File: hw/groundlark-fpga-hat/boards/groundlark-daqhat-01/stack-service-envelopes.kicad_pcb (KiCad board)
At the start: 6 copper layers, 140 x 56 mm, 190 parts, among them J1 Raspberry Pi 40-pin, J130 PI BATTERY 8-18V, J131 SWD / 3V3 REF, J4 FPGA test UART/reset, J80 LSHM-150-04.0-L-DV-A-S-K-TR, J81 LSHM-150-04.0-L-DV-A-S-K-TR, J82 LSHM-130-04.0-L-DV-A-S-K-TR, J83 12V DC / CENTER +, J90 GEO + / - / SHIELD, Q1 2N7002, Q130 2N7002, Q131 2N7002, SW80 FPGA OFF / ON, U1 24LC32A, U100 TMUX1574PWR, U101 TMUX1574PWR, U102 TCA9534PWR, U103 SN74LVC1G10DCKR, U104 TLV809EA30DBZR, U105 TLV809EA30DBZR, U106 SN74LVC1G08DCKR, U11 LSM6DSOTR, U12 LSM6DSOTR, U13 LSM6DSOTR, U130 MSPM0L1105, U131 TPS70933, U132 TPSM53603, U133 TPS22953, U22 ADS122C04, U23 DLVR-F50D, U40 TLV1117LV33DCYR, U41 SN74LVC8T245PWR, U42 SN74LVC8T245PWR, U43 ISO1640BDR, U51 TXU0202DCUR, U52 TLV803EA30DBZR, U80 TPSM53603

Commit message: Add Groundlark GNSS timing, SMA access and calibration workflow
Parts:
- added C146: 4.7u, Groundlark:Capacitor_SMD__C_0805_2012Metric, B.Cu at (71.5, 67.4)
- added C147: 100n, Groundlark:Capacitor_SMD__C_0603_1608Metric, B.Cu at (75.0, 67.4)
- added C148: 47p C0G, Groundlark:GNSS_C0402, B.Cu at (56.4, 65.8)
- added C149: 4.7u, Groundlark:Capacitor_SMD__C_0805_2012Metric, F.Cu at (70.0, 84.0)
- added C150: 4.7u, Groundlark:Capacitor_SMD__C_0805_2012Metric, F.Cu at (78.0, 84.0)
- added D140: PESD5V0F1BL, Groundlark:GNSS_SOD882, F.Cu at (54.0, 71.2)
- added J140: GNSS ANT / 3V3, Groundlark:GNSS_HL_SMA_KWE_02, F.Cu at (54.0, 65.8)
- added L140: 27n, Groundlark:GNSS_L0402, F.Cu at (54.0, 61.5)
- added TP90: GND, Groundlark:TestPoint__TestPoint_Pad_D1.5mm, B.Cu at (56.6, 97.0)
- added TP91: GEO_VCM, Groundlark:TestPoint__TestPoint_Pad_D1.5mm, B.Cu at (54.0, 97.0)
- added TP92: GEO_AVDD, Groundlark:TestPoint__TestPoint_Pad_D1.5mm, B.Cu at (57.3, 90.7)
- added TP93: GEO_DRDY_N, Groundlark:TestPoint__TestPoint_Pad_D1.5mm, B.Cu at (59.2, 88.5)
- added U140: TPS70933, Groundlark:SUP_SOT-23-5, F.Cu at (74.0, 84.0)
- added U21: MAX-M10S-00B, Groundlark:RF_GPS__ublox_MAX, B.Cu at (63.5, 62.5)
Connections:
- J1 pad 18: 18 -> GNSS_PPS
- J80 pad 18: j80-18 -> 18
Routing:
- net GNSS_BIAS: track 0.00 -> 46.1 mm, vias 0 -> 2
- net GND: track 631.4 -> 665.6 mm, vias 141 -> 145
- net PI_5V: track 490.2 -> 519.7 mm, vias 12 -> 15
- net PI_I2C_SCL: track 44.0 -> 73.4 mm, vias 4 -> 2
- net GNSS_PPS: track 0.00 -> 21.5 mm, vias 0 -> 4
- net PI_GEO_DRDY_N: track 62.8 -> 76.0 mm, vias 9 -> 7
- net PI_3V3: track 287.2 -> 298.7 mm
- net GNSS_ANT: track 0.00 -> 10.5 mm
- net PI_I2C_SDA: track 43.6 -> 52.3 mm
- net SPI_MOSI: track 94.2 -> 87.6 mm, vias 13 -> 14
- net IMU3_CS: track 62.6 -> 68.2 mm
- net FPGA_UART_TX: track 83.8 -> 88.4 mm
- net FPGA_RESET_GPIO: track 52.0 -> 56.3 mm, vias 6 -> 8
- net SENS_3V3: track 246.5 -> 242.3 mm
- net SPI_MISO: track 95.9 -> 93.6 mm, vias 20 -> 18
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
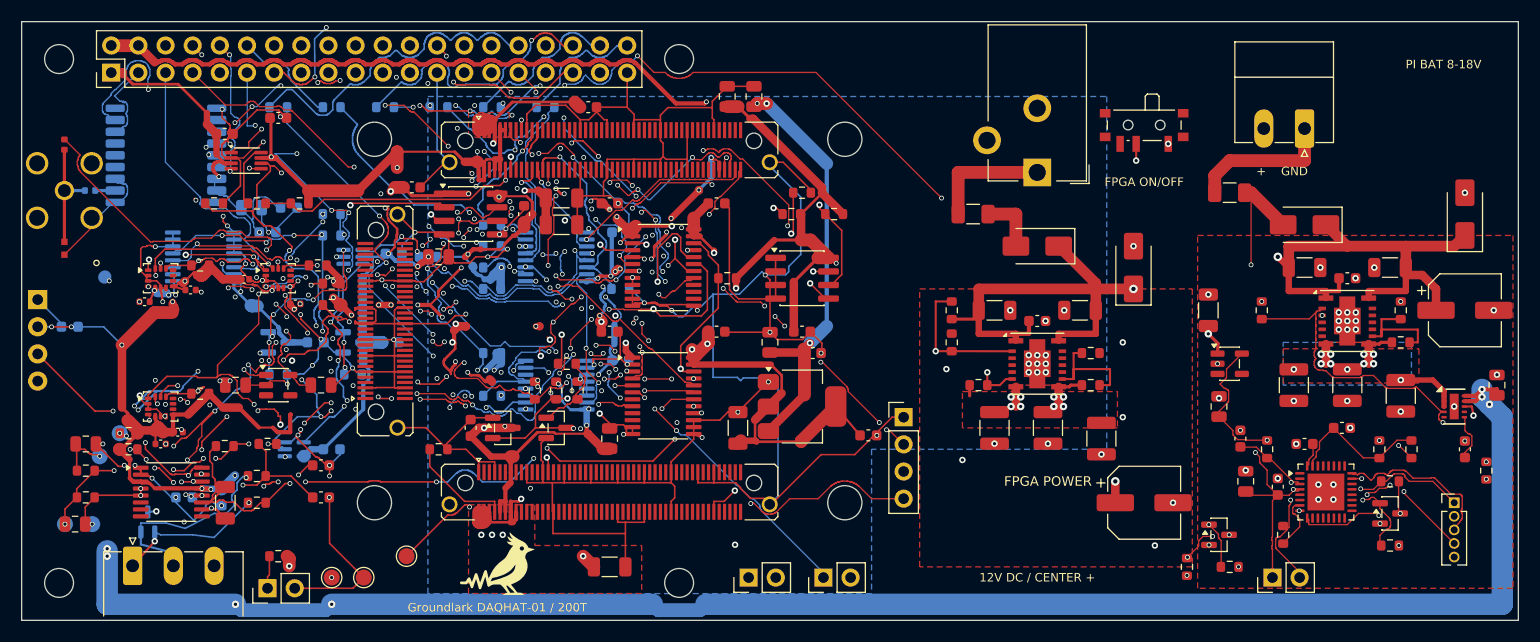
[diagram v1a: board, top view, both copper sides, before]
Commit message: Fix Groundlark power and GNSS electrical faults
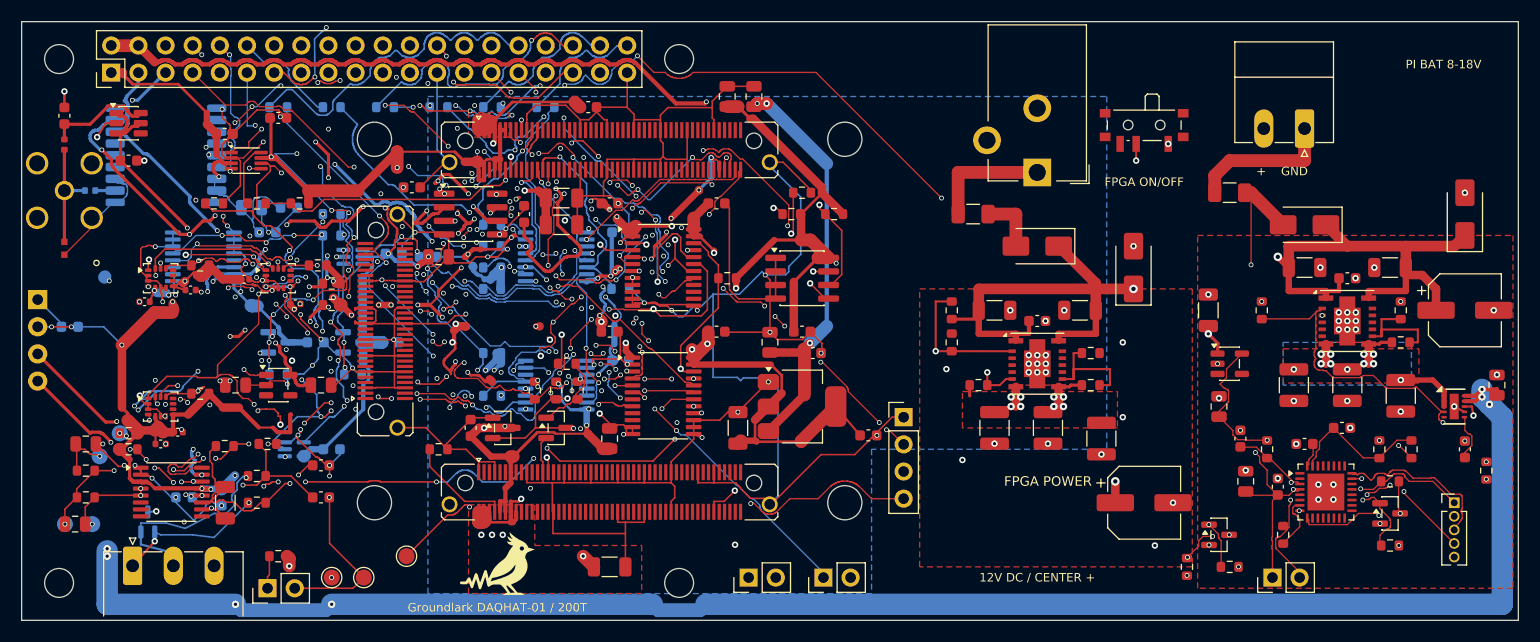
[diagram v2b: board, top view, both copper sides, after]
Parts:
- added C151: 10n, Groundlark:SUP_C_0603_1608Metric, F.Cu at (54.0, 58.8)
- added C152: 100n, Groundlark:Capacitor_SMD__C_0603_1608Metric, F.Cu at (60.0, 63.0)
- added U141: TPS2553, Groundlark:GNSS_SOT23_6, F.Cu at (60.0, 59.5)
- F130: value 4A fast -> 4A fuse
- F80: value 2A fast -> 0466002.NRHF
- R131: value 2.41k -> 2.43k
- U130: value MSPM0L1105 -> MSPM0L1106
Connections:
- C150 pad 1: GNSS_BIAS -> GNSS_LDO
- C48 pad 1: PI_3V3 -> SENS_3V3
- C49 pad 1: SENS_3V3 -> PI_3V3
- U133 pad 7: u133-7 -> GND
- U140 pad 5: GNSS_BIAS -> GNSS_LDO
- U43 pad 1: PI_3V3 -> SENS_3V3
- U43 pad 2: PI_I2C_SDA -> I2C_SDA
- U43 pad 3: PI_I2C_SCL -> I2C_SCL
- U43 pad 6: I2C_SCL -> PI_I2C_SCL
- U43 pad 7: I2C_SDA -> PI_I2C_SDA
- U43 pad 8: SENS_3V3 -> PI_3V3
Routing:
- net GNSS_LDO: track 0.00 -> 46.8 mm, vias 0 -> 5
- net GNSS_BIAS: track 46.1 -> 10.0 mm, vias 2 -> 0
- net PI_I2C_SDA: track 52.3 -> 81.4 mm, vias 2 -> 8
- net PI_3V3: track 298.7 -> 320.2 mm, vias 20 -> 24
- net I2C_SCL: track 69.7 -> 85.0 mm
- net SENS_3V3: track 242.3 -> 250.1 mm, vias 36 -> 42
- net GND: track 665.6 -> 671.4 mm, vias 145 -> 148
- net I2C_SDA: track 70.7 -> 66.7 mm, vias 14 -> 8
- net PI_I2C_SCL: track 73.4 -> 75.8 mm, vias 2 -> 9
